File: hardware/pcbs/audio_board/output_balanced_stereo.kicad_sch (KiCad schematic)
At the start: 48 parts, among them J5 NC3MAH, J8 NC3MAH, U11 NE5532, U12 NE5532, U7 NE5532

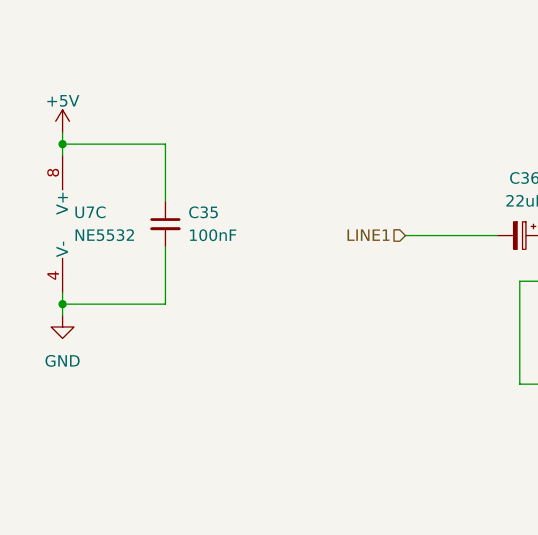
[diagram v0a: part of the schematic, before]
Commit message: audio_board: Rework for DECT plug-in module
Redesigned the DECT area to accept a daughterboard with whatever DECT
module ends up working. Added more holes and silkscreen to make the
board neater.
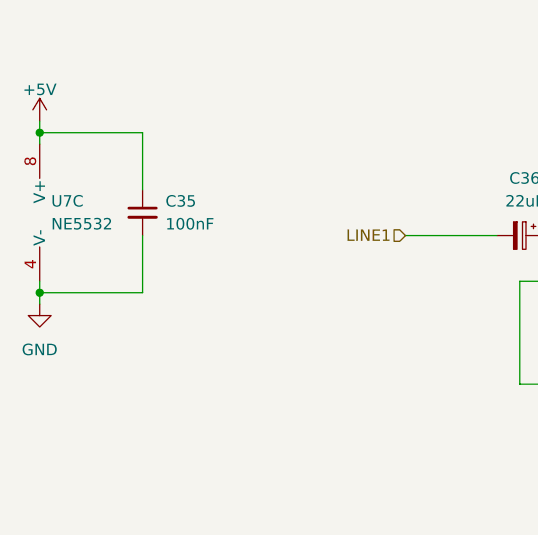
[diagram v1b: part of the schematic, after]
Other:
- moved on the sheet: C35, U7C
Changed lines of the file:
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@@
 	)
 	(junction
-		(at 35.56 39.37)
+		(at 33.02 38.1)
 		(diameter 0)
 		(color 0 0 0 0)
@@
 	)
 	(junction
-		(at 35.56 57.15)
+		(at 33.02 55.88)
 		(diameter 0)
 		(color 0 0 0 0)
@@
 	(wire
 		(pts
-			(xy 35.56 40.64) (xy 35.56 39.37)
+			(xy 33.02 39.37) (xy 33.02 38.1)
 		)
 		(stroke
@@
 	(wire
 		(pts
-			(xy 46.99 39.37) (xy 46.99 45.72)
+			(xy 44.45 38.1) (xy 44.45 44.45)
 		)
 		(stroke
@@
 	(wire
 		(pts
-			(xy 35.56 55.88) (xy 35.56 57.15)
+			(xy 33.02 54.61) (xy 33.02 55.88)
 		)
 		(stroke
@@
 	(wire
 		(pts
-			(xy 35.56 38.1) (xy 35.56 39.37)
+			(xy 33.02 36.83) (xy 33.02 38.1)
 		)
 		(stroke
@@
 	(wire
 		(pts
-			(xy 35.56 57.15) (xy 46.99 57.15)
+			(xy 33.02 55.88) (xy 44.45 55.88)
 		)
 		(stroke
@@
 	(wire
 		(pts
-			(xy 46.99 50.8) (xy 46.99 57.15)
+			(xy 44.45 49.53) (xy 44.45 55.88)
 		)
 		(stroke
@@
 	(wire
 		(pts
-			(xy 35.56 39.37) (xy 46.99 39.37)
+			(xy 33.02 38.1) (xy 44.45 38.1)
 		)
 		(stroke
@@
 	(wire
 		(pts
-			(xy 35.56 58.42) (xy 35.56 57.15)
+			(xy 33.02 57.15) (xy 33.02 55.88)
 		)
 		(stroke
@@
 	(symbol
 		(lib_id "power:+5V")
-		(at 35.56 38.1 0)
+		(at 33.02 36.83 0)
 		(unit 1)
 		(exclude_from_sim no)
@@
 		(fields_autoplaced yes)
 		(property "Reference" "#PWR028"
-			(at 35.56 41.91 0)
+			(at 33.02 40.64 0)
 			(effects
 				(font
@@
 		)
 		(property "Value" "+5V"
-			(at 35.56 34.5981 0)
+			(at 33.02 33.3281 0)
 			(effects
 				(font
@@
 		)
 		(property "Footprint" ""
-			(at 35.56 38.1 0)
+			(at 33.02 36.83 0)
 			(effects
 				(font
@@
 		)
 		(property "Datasheet" ""
-			(at 35.56 38.1 0)
+			(at 33.02 36.83 0)
 			(effects
 				(font
@@
 		)
 		(property "Description" ""
-			(at 35.56 38.1 0)
+			(at 33.02 36.83 0)
 			(effects
 				(font
@@
 	(symbol
 		(lib_id "power:GND")
-		(at 35.56 58.42 0)
+		(at 33.02 57.15 0)
 		(unit 1)
 		(exclude_from_sim no)
@@
 		(fields_autoplaced yes)
 		(property "Reference" "#PWR026"
-			(at 35.56 64.77 0)
+			(at 33.02 63.5 0)
 			(effects
 				(font
@@
 		)
 		(property "Value" "GND"
-			(at 35.56 63.5 0)
+			(at 33.02 62.23 0)
 			(effects
 				(font
@@
 		)
 		(property "Footprint" ""
-			(at 35.56 58.42 0)
+			(at 33.02 57.15 0)
 			(effects
 				(font
@@
 		)
 		(property "Datasheet" ""
-			(at 35.56 58.42 0)
+			(at 33.02 57.15 0)
 			(effects
 				(font
@@
 		)
 		(property "Description" "Power symbol creates a global label with name \"GND\" , ground"
-			(at 35.56 58.42 0)
+			(at 33.02 57.15 0)
 			(effects
 				(font
@@
 	(symbol
 		(lib_id "Device:C_Small")
-		(at 46.99 48.26 0)
+		(at 44.45 46.99 0)
 		(unit 1)
 		(exclude_from_sim no)
@@
 		(fields_autoplaced yes)
 		(property "Reference" "C35"
-			(at 49.53 46.9962 0)
+			(at 46.99 45.7262 0)
 			(effects
 				(font
@@
 		)
 		(property "Value" "100nF"
-			(at 49.53 49.5362 0)
+			(at 46.99 48.2662 0)
 			(effects
 				(font
@@
 		)
 		(property "Footprint" "Capacitor_SMD:C_0603_1608Metric"
-			(at 46.99 48.26 0)
+			(at 44.45 46.99 0)
 			(effects
 				(font
@@
 		)
 		(property "Datasheet" "~"
-			(at 46.99 48.26 0)
+			(at 44.45 46.99 0)
 			(effects
 				(font
@@
 		)
 		(property "Description" "Unpolarized capacitor, small symbol"
-			(at 46.99 48.26 0)
+			(at 44.45 46.99 0)
 			(effects
 				(font
@@
 		)
 		(property "LCSC" "C14663"
-			(at 46.99 48.26 0)
+			(at 44.45 46.99 0)
 			(effects
 				(font
@@
 		)
 		(property "MPN" "885012206046"
-			(at 46.99 48.26 0)
+			(at 44.45 46.99 0)
 			(effects
 				(font
@@
 	(symbol
 		(lib_id "Amplifier_Operational:NE5532")
-		(at 38.1 48.26 0)
+		(at 35.56 46.99 0)
 		(unit 3)
 		(exclude_from_sim no)
@@
 		(fields_autoplaced yes)
 		(property "Reference" "U7"
-			(at 36.83 46.9899 0)
+			(at 34.29 45.7199 0)
 			(effects
 				(font
@@
 		)
 		(property "Value" "NE5532"
-			(at 36.83 49.5299 0)
+			(at 34.29 48.2599 0)
 			(effects
 				(font
@@
 		)
 		(property "Footprint" "Package_SO:SOIC-8_3.9x4.9mm_P1.27mm"
-			(at 38.1 48.26 0)
+			(at 35.56 46.99 0)
 			(effects
 				(font
@@
 		)
 		(property "Datasheet" "http://www.ti.com/lit/ds/symlink/ne5532.pdf"
-			(at 38.1 48.26 0)
+			(at 35.56 46.99 0)
 			(effects
 				(font
@@
 		)
 		(property "Description" "Dual Low-Noise Operational Amplifiers, DIP-8/SOIC-8"
-			(at 38.1 48.26 0)
+			(at 35.56 46.99 0)
 			(effects
 				(font
@@
 		)
 		(property "LCSC" "C7426"
-			(at 38.1 48.26 0)
+			(at 35.56 46.99 0)
 			(effects
 				(font
@@
 		)
 		(property "MPN" ""
-			(at 38.1 48.26 0)
+			(at 35.56 46.99 0)
 			(effects
 				(font

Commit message: audio_board, power_board: update shop and part links
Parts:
- C24, C25, C50, C51: Part (none) -> C 100pF 16V 0603
- C35, C47, C49, C56, C58: Part (none) -> C 100nF 16V 0603
- C36, C44, C46, C52, C53, C54: Part (none) -> C 22uF 16V 0805
- C48, C57: Part (none) -> C 10μ 16V 0805
- J5, J8: Part (none) -> NC3MAH; Shop (none) -> https://eu.mouser.com/ProductDetail/568-NC3MAH
- R23, R44: Part (none) -> R 6.81kΩ 0603
- R27, R29, R30, R35, R41, R42, R45, R46, R47, R52, R57, R58: Part (none) -> R 10kΩ 0603
- R31, R32, R36, R43, R48, R49, R56, R61: Part (none) -> R 22kΩ 0603
- R33, R34, R50, R51: Part (none) -> R 47Ω 0603
- U11, U12, U7: Part (none) -> NE5532DR; Shop (none) -> https://store.comet.bg/Catalogue/Product/17010/

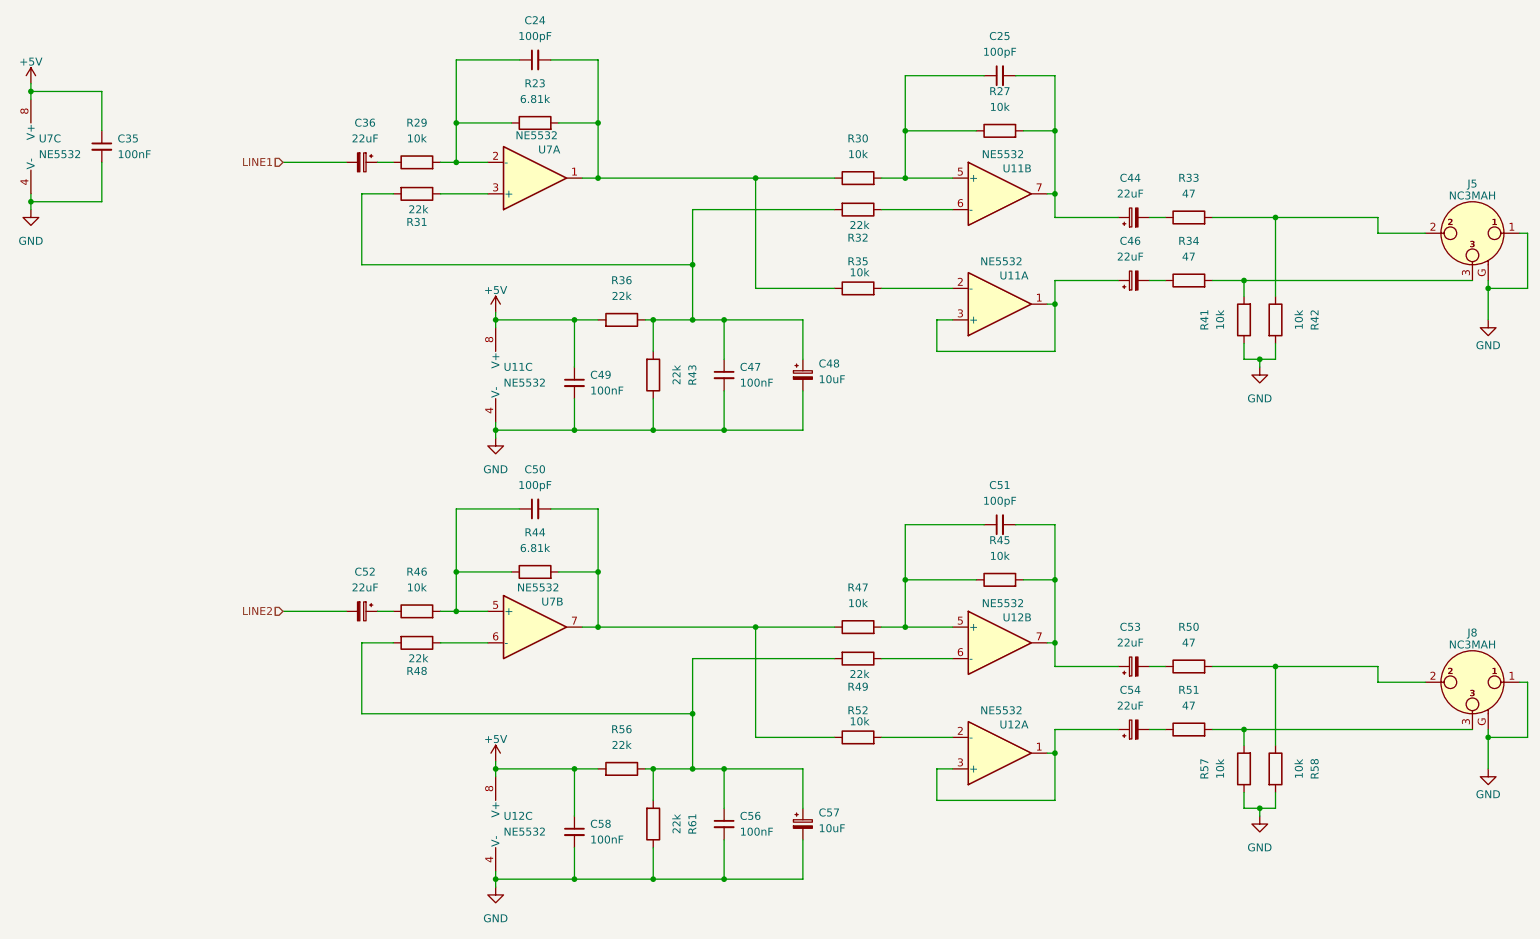
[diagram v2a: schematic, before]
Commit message: Audio board revision C
* Switched the neutrik jacks to NC3FAH2 instead of FAH1 so the jacks
  with an extra ground pin fit (but the FAH1 ones also still fit)
* Added traces for optional leds (marked DNP)
* Fixed up the opamp orientation for the XLR outputs
* Moved the LCD connector to the other side of the board and switched to
  an MTA-100 connector
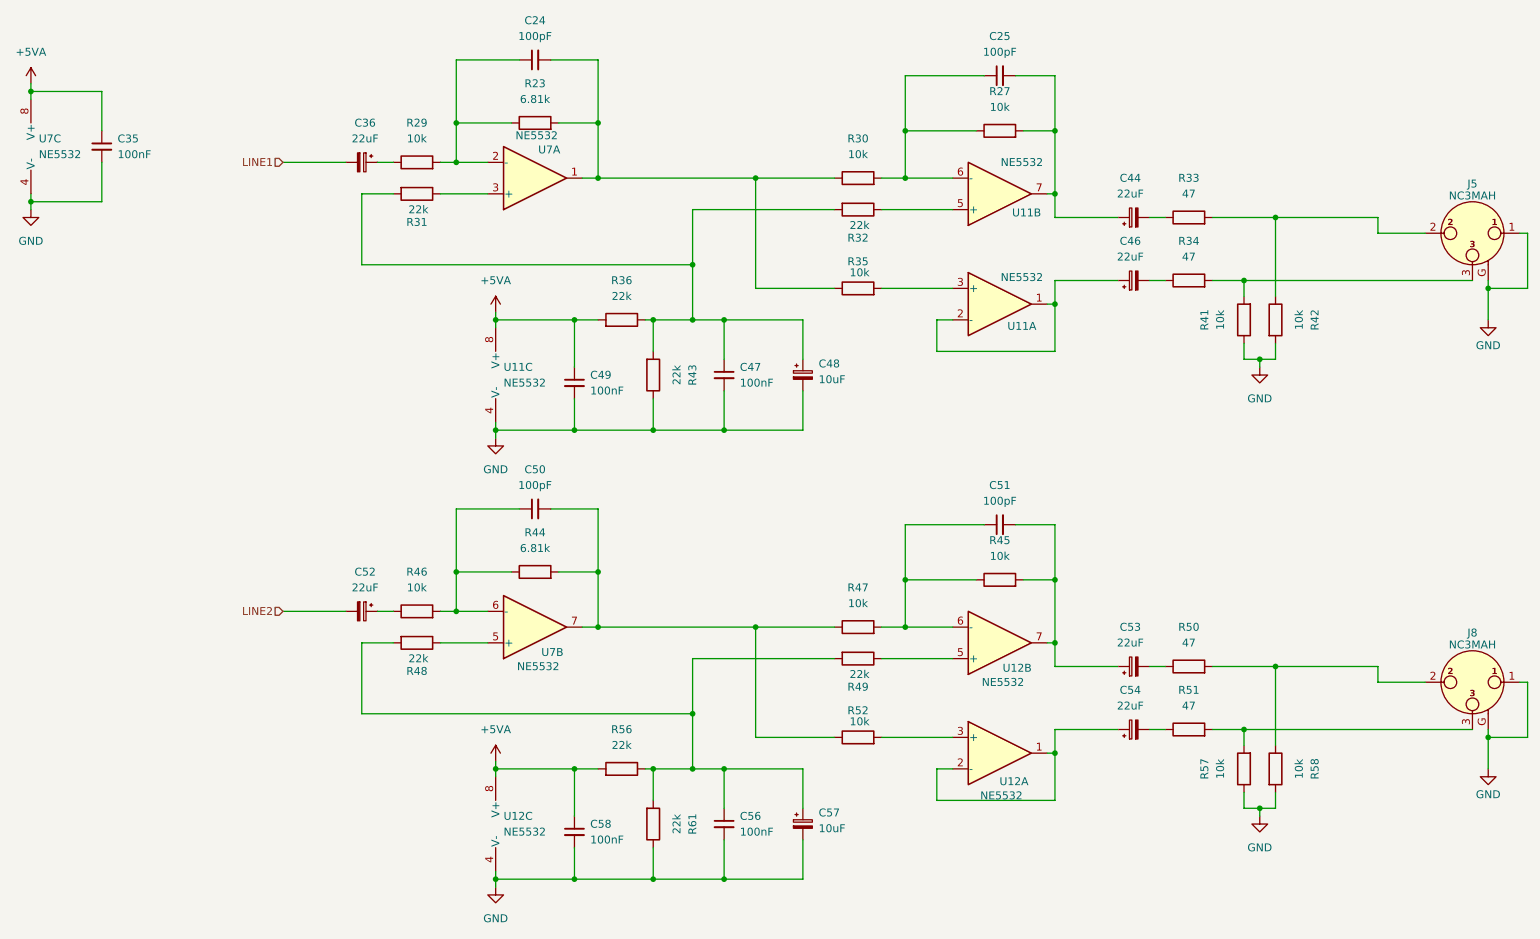
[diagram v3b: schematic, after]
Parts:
- C24, C25, C50, C51: Part C 100pF 16V 0603 -> (none)
- C35, C47, C49, C56, C58: Part C 100nF 16V 0603 -> (none)
- C36, C44, C46, C52, C53, C54: Part C 22uF 16V 0805 -> (none)
- C48, C57: Part C 10μ 16V 0805 -> (none)
- J5, J8: Part NC3MAH -> (none); Shop https://eu.mouser.com/ProductDetail/568-NC3MAH -> (none)
- R23, R44: Part R 6.81kΩ 0603 -> (none)
- R27, R29, R30, R35, R41, R42, R45, R46, R47, R52, R57, R58: Part R 10kΩ 0603 -> (none)
- R31, R32, R36, R43, R48, R49, R56, R61: Part R 22kΩ 0603 -> (none)
- R33, R34, R50, R51: Part R 47Ω 0603 -> (none)
- U11, U12, U7: Part NE5532DR -> (none); Shop https://store.comet.bg/Catalogue/Product/17010/ -> (none)
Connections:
- net at C51.1, R45.1, R47.2: now also U12.6 (-); no longer U12.5 (+)
- net at R32.1: now also U11.5 (+); no longer U11.6 (-)
- net at C50.1, R44.1, R46.2: now also U7.6 (-); no longer U7.5 (+)
- net at C25.1, R27.1, R30.2: now also U11.6 (-); no longer U11.5 (+)
- net at C46.1, U11.1: now also U11.2 (-); no longer U11.3 (+)
- net at R35.2: now also U11.3 (+); no longer U11.2 (-)
- net at R52.2: now also U12.3 (+); no longer U12.2 (-)
- net at R49.1: now also U12.5 (+); no longer U12.6 (-)
- net at R48.1: now also U7.5 (+); no longer U7.6 (-)
- net at C54.1, U12.1: now also U12.2 (-); no longer U12.3 (+)
- net +5V renamed +5VA

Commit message: Audio board Rev. C fixes
* Switch opamp to OPA1678
* Fix filter resistor on inputs from 22 ohm to 220 ohm
* Make the board 4 layers for a better ground plane
* Implement an RC filter for the opamp 5V line
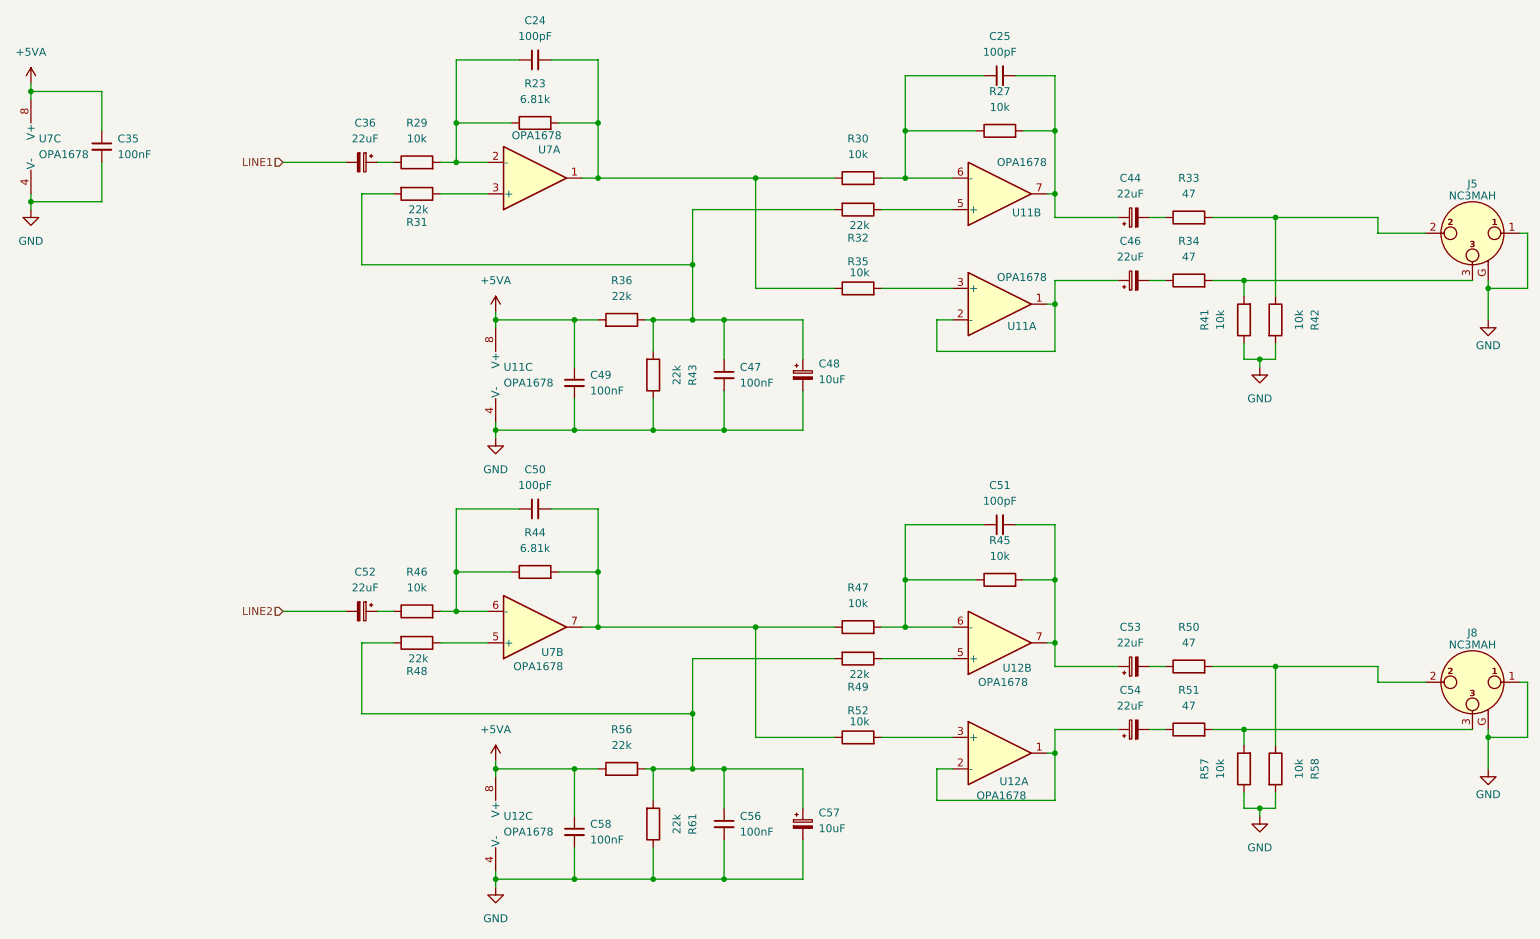
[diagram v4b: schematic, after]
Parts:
- U11, U12, U7: value NE5532 -> OPA1678; LCSC C7426 -> C192421; MPN (none) -> 595-OPA1678IDR
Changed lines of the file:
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@@
 			)
 		)
-		(property "Value" "NE5532"
+		(property "Value" "OPA1678 "
 			(at 114.554 45.212 0)
 			(effects
@@
 			)
 		)
-		(property "LCSC" "C7426"
+		(property "LCSC" "C192421"
 			(at 114.3 52.07 0)
 			(effects
@@
 			)
 		)
-		(property "MPN" ""
+		(property "MPN" "595-OPA1678IDR "
 			(at 114.3 52.07 0)
 			(effects
@@
 			)
 		)
-		(property "Value" "NE5532"
+		(property "Value" "OPA1678 "
 			(at 109.22 85.0899 0)
 			(effects
@@
 			)
 		)
-		(property "LCSC" "C7426"
+		(property "LCSC" "C192421"
 			(at 110.49 83.82 0)
 			(effects
@@
 			)
 		)
-		(property "MPN" ""
+		(property "MPN" "595-OPA1678IDR "
 			(at 110.49 83.82 0)
 			(effects
@@
 			)
 		)
-		(property "Value" "NE5532"
+		(property "Value" "OPA1678 "
 			(at 192.786 49.53 0)
 			(effects
@@
 			)
 		)
-		(property "LCSC" "C7426"
+		(property "LCSC" "C192421"
 			(at 189.23 54.61 0)
 			(effects
@@
 			)
 		)
-		(property "MPN" ""
+		(property "MPN" "595-OPA1678IDR "
 			(at 189.23 54.61 0)
 			(effects
@@
 			)
 		)
-		(property "Value" "NE5532"
+		(property "Value" "OPA1678 "
 			(at 192.786 68.072 0)
 			(effects
@@
 			)
 		)
-		(property "LCSC" "C7426"
+		(property "LCSC" "C192421"
 			(at 189.23 72.39 0)
 			(effects
@@
 			)
 		)
-		(property "MPN" ""
+		(property "MPN" "595-OPA1678IDR "
 			(at 189.23 72.39 0)
 			(effects
@@
 			)
 		)
-		(property "Value" "NE5532"
+		(property "Value" "OPA1678 "
 			(at 109.22 157.4799 0)
 			(effects
@@
 			)
 		)
-		(property "LCSC" "C7426"
+		(property "LCSC" "C192421"
 			(at 110.49 156.21 0)
 			(effects
@@
 			)
 		)
-		(property "MPN" ""
+		(property "MPN" "595-OPA1678IDR "
 			(at 110.49 156.21 0)
 			(effects
@@
 			)
 		)
-		(property "Value" "NE5532"
+		(property "Value" "OPA1678 "
 			(at 34.29 48.2599 0)
 			(effects
@@
 			)
 		)
-		(property "LCSC" "C7426"
+		(property "LCSC" "C192421"
 			(at 35.56 46.99 0)
 			(effects
@@
 			)
 		)
-		(property "MPN" ""
+		(property "MPN" "595-OPA1678IDR "
 			(at 35.56 46.99 0)
 			(effects
@@
 			)
 		)
-		(property "Value" "NE5532"
+		(property "Value" "OPA1678 "
 			(at 189.738 133.35 0)
 			(effects
@@
 			)
 		)
-		(property "LCSC" "C7426"
+		(property "LCSC" "C192421"
 			(at 189.23 127 0)
 			(effects
@@
 			)
 		)
-		(property "MPN" ""
+		(property "MPN" "595-OPA1678IDR "
 			(at 189.23 127 0)
 			(effects
@@
 			)
 		)
-		(property "Value" "NE5532"
+		(property "Value" "OPA1678 "
 			(at 114.808 130.81 0)
 			(effects
@@
 			)
 		)
-		(property "LCSC" "C7426"
+		(property "LCSC" "C192421"
 			(at 114.3 124.46 0)
 			(effects
@@
 			)
 		)
-		(property "MPN" ""
+		(property "MPN" "595-OPA1678IDR "
 			(at 114.3 124.46 0)
 			(effects
@@
 			)
 		)
-		(property "Value" "NE5532"
+		(property "Value" "OPA1678 "
 			(at 189.484 151.638 0)
 			(effects
@@
 			)
 		)
-		(property "LCSC" "C7426"
+		(property "LCSC" "C192421"
 			(at 189.23 144.78 0)
 			(effects
@@
 			)
 		)
-		(property "MPN" ""
+		(property "MPN" "595-OPA1678IDR "
 			(at 189.23 144.78 0)
 			(effects

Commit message: pcbs: update purchase info
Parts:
- C24, C25, C50, C51: Part (none) -> C 100pF 16V 0603; Shop (none) -> https://store.comet.bg/Catalogue/Product/37094/
- C35, C47, C49, C56, C58: Part (none) -> C 100nF 16V 0603; Shop (none) -> https://store.comet.bg/Catalogue/Product/38000/
- C36, C44, C46, C52, C53, C54: Part (none) -> C 22μF 16V 0805; Shop (none) -> https://store.comet.bg/Catalogue/Product/9624/
- C48, C57: Part (none) -> C 10μF 16V 0805; Shop (none) -> https://store.comet.bg/Catalogue/Product/36934/
- J5, J8: Part (none) -> NC3MAH; Shop (none) -> https://eu.mouser.com/ProductDetail/Neutrik/NC3MAH?qs=MO8z%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
- R23, R44: Part (none) -> R 6.81kΩ 125mW 1% 0603; Shop (none) -> https://www.tme.eu/lv/en/details/crcw06036k81fktabc/smd-res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
- R27, R29, R30, R35, R41, R42, R45, R46, R47, R52, R57, R58: Part (none) -> R 10kΩ 125mW 1% 0603; Shop (none) -> https://store.comet.bg/Catalogue/Product/4415/
- R31, R32, R36, R43, R48, R49, R56, R61: Part (none) -> R 22kΩ 125mW 1% 0603; Shop (none) -> https://store.comet.bg/Catalogue/Product/4419/
- R33, R34, R50, R51: Part (none) -> R 47Ω 125mW 1% 0603; Shop (none) -> https://store.comet.bg/Catalogue/Product/4392/
- U11, U12, U7: value OPA1678 -> OPA1678; Part (none) -> OPA1678IDR; Shop (none) -> https://eu.mouser.com/ProductDetail/Texas-Instruments/OPA16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

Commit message: boards: fix minor bom issues
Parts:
- C36, C44, C46, C52, C53, C54: Part C 22μF 16V 0805 -> C 22μF 25V 0805
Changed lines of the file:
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@@
 			)
 		)
-		(property "Part" "C 22μF 16V 0805"
+		(property "Part" "C 22μF 25V 0805"
 			(at 210.82 130.81 0)
 			(effects
@@
 			)
 		)
-		(property "Part" "C 22μF 16V 0805"
+		(property "Part" "C 22μF 25V 0805"
 			(at 86.36 49.53 0)
 			(effects
@@
 			)
 		)
-		(property "Part" "C 22μF 16V 0805"
+		(property "Part" "C 22μF 25V 0805"
 			(at 210.82 68.58 0)
 			(effects
@@
 			)
 		)
-		(property "Part" "C 22μF 16V 0805"
+		(property "Part" "C 22μF 25V 0805"
 			(at 86.36 121.92 0)
 			(effects
@@
 			)
 		)
-		(property "Part" "C 22μF 16V 0805"
+		(property "Part" "C 22μF 25V 0805"
 			(at 210.82 140.97 0)
 			(effects
@@
 			)
 		)
-		(property "Part" "C 22μF 16V 0805"
+		(property "Part" "C 22μF 25V 0805"
 			(at 210.82 58.42 0)
 			(effects
